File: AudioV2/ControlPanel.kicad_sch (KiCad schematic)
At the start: 39 parts, among them SW1 PWR SW, SW501 DEST sense (3PDT 3rd pole), U501 Pico 2 / RP2350, U502 PT2314-D, U503 BP5293-50 +5V

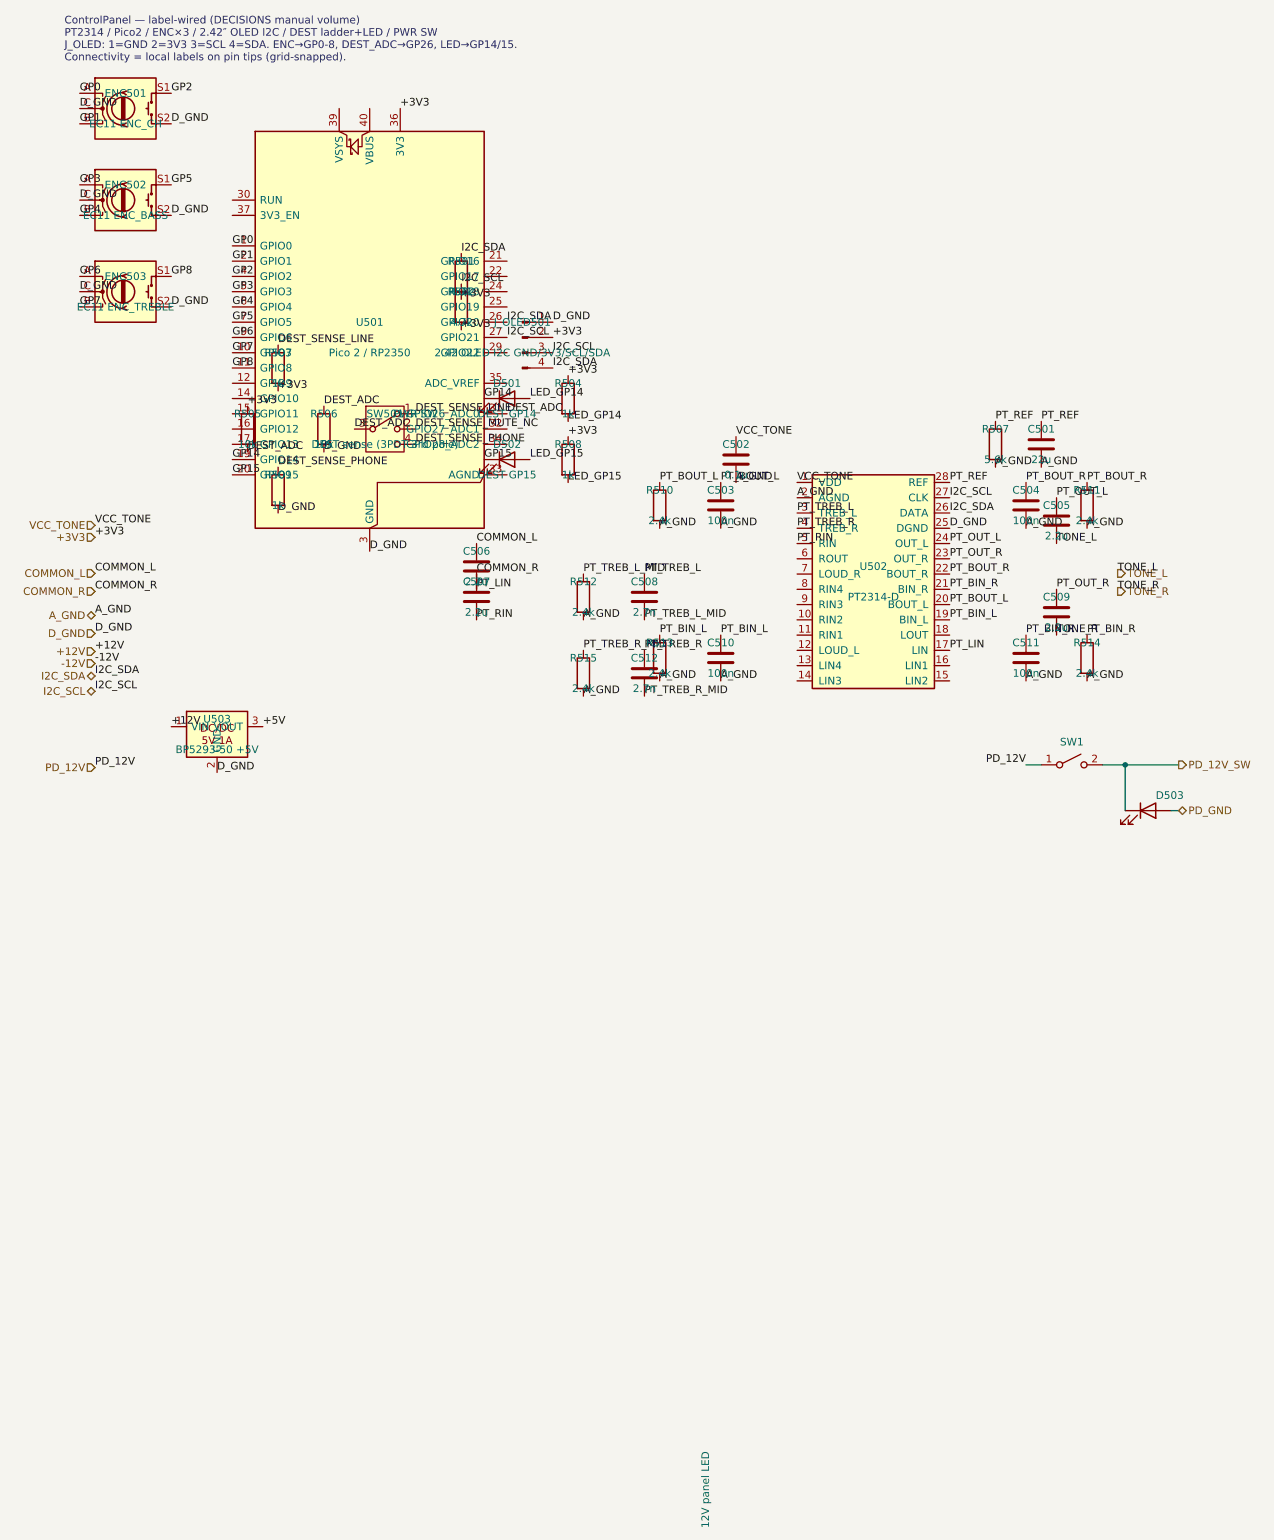
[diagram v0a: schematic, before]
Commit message: AudioV2: Amp再版とRelayBoard本配線、番地ストラップを0Ω化
高速オペアンプを差せるようAmpをバルク対応で再版した（ゲイン2＝20k/20k、
±12V、100µF/rail + 100nF + 1nF、DIP-8ソケット）。親には代表1シートだけ置き、
物理は同一仕様×10製造とする。PCBは既存基板の端子・4穴を維持したまま上辺を
15mm拡張してバルクを載せた。

RelayBoardは未給電Ampへ信号を印加しないよう、Amp入力と±12Vを同一の
SET/RESETで同時切替する構成で本配線した。番地はA1/A0の0Ωストラップで
0x20–0x23を選び、1枚のPCB設計を最大4枚に使い回す。SolderJumperは
FPが1.3mmピッチで0Ωチップが載らないため1206パッドに変更した。
プルダウン10kΩはジャンパ後段に置き常時実装（手前分岐だと未実装時に
A0/A1が浮く）。

ERC 207→56。Power/Output/Amp/Relay A・B は0件で、残りはControlの
未使用ピンと親の箱外ラベル。AmpのPCB DRCは電気エラー0・未配線0。

レビュー指摘（IC直近パスコン、AZ850のset voltage余裕、A0/A1ネット無名）は
未対応でAGENT_HANDOFF §2.7に記録。addr_strapのスクリプト側は現図と
非同期なので、同期までwire_circuit_design.py relayを回さない。

Co-authored-by: Cursor <cursoragent@cursor.com>
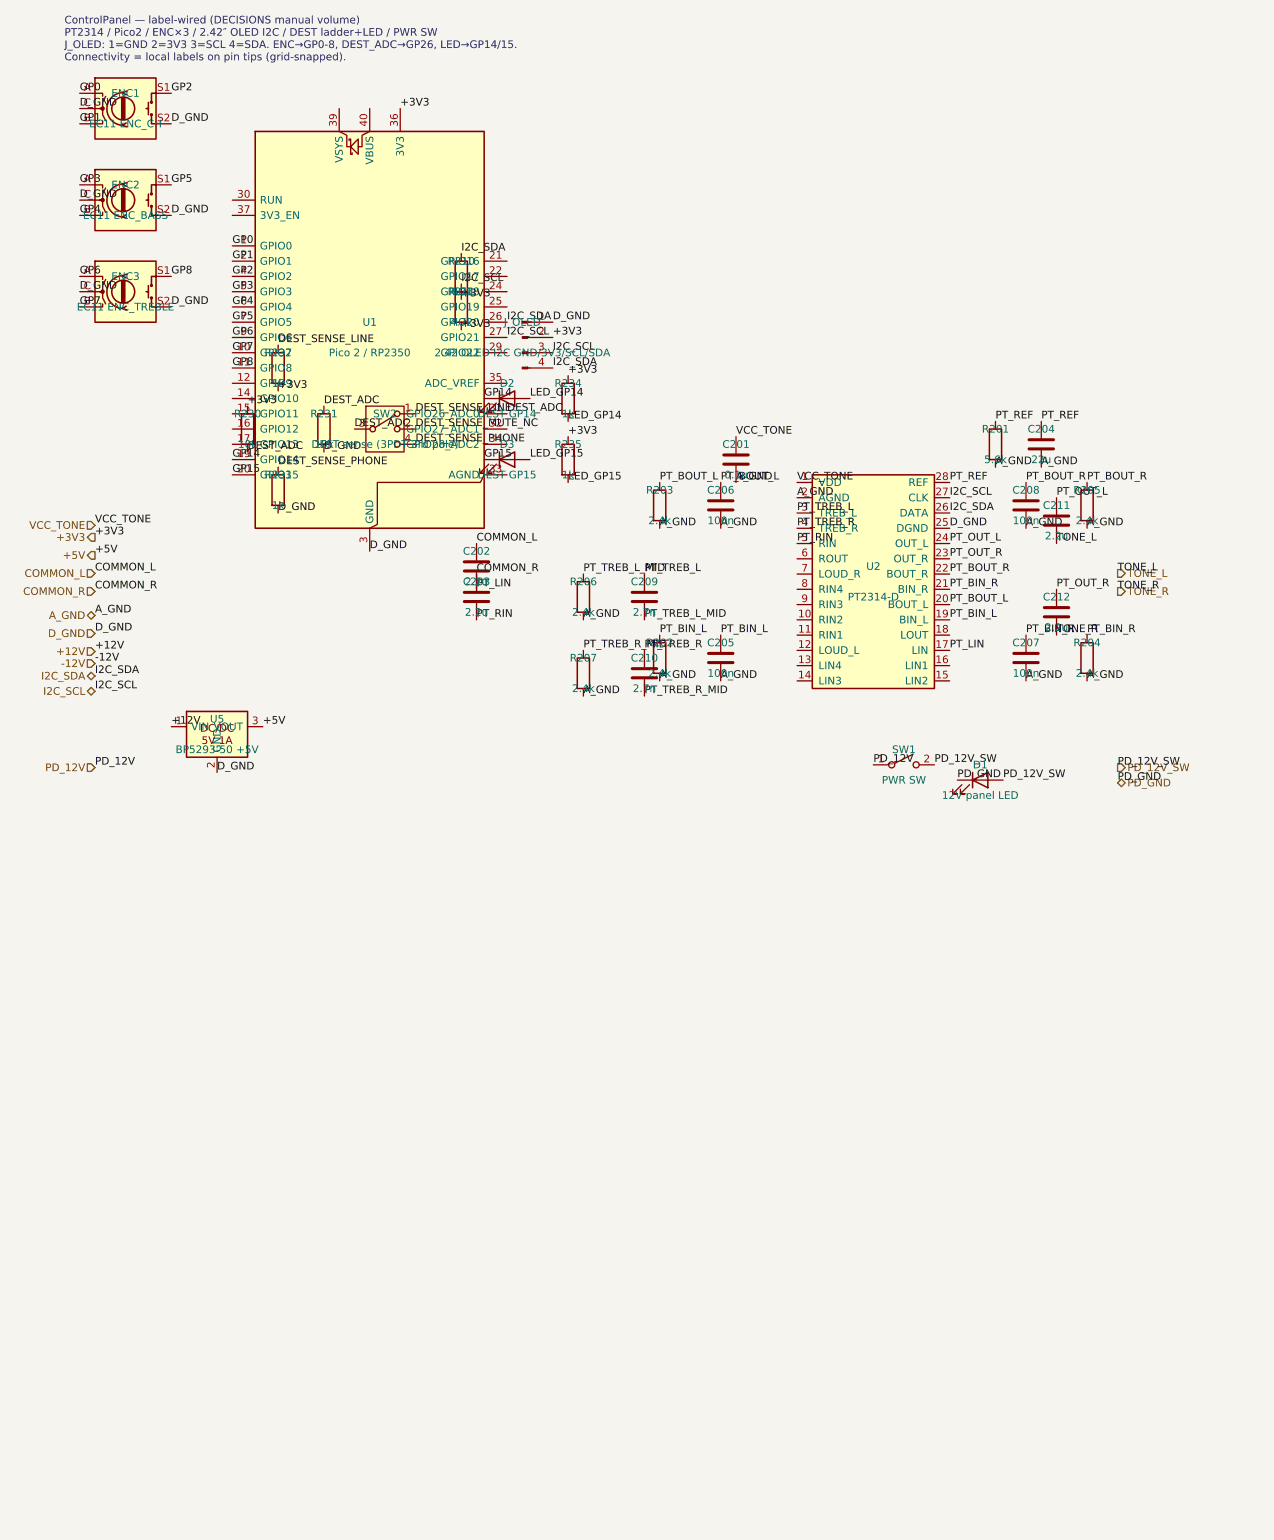
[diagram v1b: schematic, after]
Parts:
- removed C501: 22u, symbol Device:C
- removed C502: 0.1u, symbol Device:C
- removed C503, C504, C510, C511: 100n, symbol Device:C
- removed C505, C506, C507, C509: 2.2u, symbol Device:C
- removed C508, C512: 2.7n, symbol Device:C
- removed D501: DEST GP14, symbol Device:LED
- removed D502: DEST GP15, symbol Device:LED
- removed D503: 12V panel LED, symbol Device:LED
- removed ENC501: EC11 ENC_CH, symbol Device:RotaryEncoder_Switch
- removed ENC502: EC11 ENC_BASS, symbol Device:RotaryEncoder_Switch
- removed ENC503: EC11 ENC_TREBLE, symbol Device:RotaryEncoder_Switch
- removed J_OLED501: 2.42 OLED I2C GND/3V3/SCL/SDA, symbol Connector:Conn_01x04_Pin
- removed R501, R502: 4.7k, symbol Device:R
- removed R503, R504, R508, R509: 1k, symbol Device:R
- removed R505, R506: 10k, symbol Device:R
- removed R507: 5.6k, symbol Device:R
- removed R510, R511, R512, R513, R514, R515: 2.4k, symbol Device:R
- removed SW501: DEST sense (3PDT 3rd pole), symbol Switch:SW_SP3T
- removed U501: Pico 2 / RP2350, symbol MCU_Module:RaspberryPi_Pico
- removed U502: PT2314-D, symbol AudioV2:PT2314
- removed U503: BP5293-50 +5V, symbol BP5293_ROHM:BP5293-50
- added C201: 0.1u, symbol Device:C
- added C202, C203, C211, C212: 2.2u, symbol Device:C
- added C204: 22u, symbol Device:C
- added C205, C206, C207, C208: 100n, symbol Device:C
- added C209, C210: 2.7n, symbol Device:C
- added D1: 12V panel LED, symbol Device:LED
- added D2: DEST GP14, symbol Device:LED
- added D3: DEST GP15, symbol Device:LED
- added ENC1: EC11 ENC_CH, symbol Device:RotaryEncoder_Switch
- added ENC2: EC11 ENC_BASS, symbol Device:RotaryEncoder_Switch
- added ENC3: EC11 ENC_TREBLE, symbol Device:RotaryEncoder_Switch
- added J_OLED: 2.42 OLED I2C GND/3V3/SCL/SDA, symbol Connector:Conn_01x04_Pin
- added R201: 5.6k, symbol Device:R
- added R202, R203, R204, R205, R206, R207: 2.4k, symbol Device:R
- added R210, R211: 4.7k, symbol Device:R
- added R230, R231: 10k, symbol Device:R
- added R232, R233, R234, R235: 1k, symbol Device:R
- added SW2: DEST sense (3PDT 3rd pole), symbol Switch:SW_SP3T
- added U1: Pico 2 / RP2350, symbol MCU_Module:RaspberryPi_Pico
- added U2: PT2314-D, symbol AudioV2:PT2314
- added U5: BP5293-50 +5V, symbol BP5293_ROHM:BP5293-50
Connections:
- net +12V: now also U5.1 (VIN)
- net +3V3: now also J_OLED.2 (Pin_2), R210.2, R211.2, R230.1, R232.2, R234.1, R235.1, U1.36 (3V3)
- net +5V: now also U5.3 (VOUT)
- net A_GND: now also C201.2, C204.2, C205.2, C206.2, C207.2, C208.2, R201.2, R202.2, R203.2, R204.2, R205.2, R206.2, R207.2, U2.2 (AGND)
- net COMMON_L: now also C202.1
- net COMMON_R: now also C203.1
- net DEST_ADC: now also R230.2, R231.1, SW2.3, U1.31 (GPIO26_ADC0)
- net DEST_SENSE_LINE: now also R232.1, SW2.1
- net DEST_SENSE_MUTE_NC: now also SW2.2
- net DEST_SENSE_PHONE: now also R233.1, SW2.4
- net D_GND: now also ENC1.C, ENC1.S2, ENC2.C, ENC2.S2, ENC3.C, ENC3.S2, J_OLED.1 (Pin_1), R231.2, R233.2, U1.13 (GND), U1.18 (GND), U1.23 (GND), U1.28 (GND), U1.3 (GND), U1.38 (GND), U1.8 (GND), U2.25 (DGND), U5.2 (GND)
- net GP0: now also ENC1.A, U1.1 (GPIO0)
- net GP1: now also ENC1.B, U1.2 (GPIO1)
- net GP14: now also D2.1 (K), U1.19 (GPIO14)
- net GP15: now also D3.1 (K), U1.20 (GPIO15)
- net GP2: now also ENC1.S1, U1.4 (GPIO2)
- net GP3: now also ENC2.A, U1.5 (GPIO3)
- net GP4: now also ENC2.B, U1.6 (GPIO4)
- net GP5: now also ENC2.S1, U1.7 (GPIO5)
- net GP6: now also ENC3.A, U1.9 (GPIO6)
- net GP7: now also ENC3.B, U1.10 (GPIO7)
- net GP8: now also ENC3.S1, U1.11 (GPIO8)
- net I2C_SCL: now also J_OLED.3 (Pin_3), R211.1, U1.27 (GPIO21), U2.27 (CLK)
- net I2C_SDA: now also J_OLED.4 (Pin_4), R210.1, U1.26 (GPIO20), U2.26 (DATA)
- net LED_GP14: now also D2.2 (A), R234.2
- net LED_GP15: now also D3.2 (A), R235.2
- net PD_12V_SW: now also D1.2 (A)
- net PD_GND: now also D1.1 (K)
- net PT_BIN_L: now also C205.1, R202.1, U2.19 (BIN_L)
- net PT_BIN_R: now also C207.1, R204.1, U2.21 (BIN_R)
- net PT_BOUT_L: now also C206.1, R203.1, U2.20 (BOUT_L)
- net PT_BOUT_R: now also C208.1, R205.1, U2.22 (BOUT_R)
- net PT_LIN: now also C202.2, U2.17 (LIN)
- net PT_OUT_L: now also C211.1, U2.24 (OUT_L)
- net PT_OUT_R: now also C212.1, U2.23 (OUT_R)
- net PT_REF: now also C204.1, R201.1, U2.28 (REF)
- net PT_RIN: now also C203.2, U2.5 (RIN)
- net PT_TREB_L: now also C209.1, U2.3 (TREB_L)
- net PT_TREB_L_MID: now also C209.2, R206.1
- net PT_TREB_R: now also C210.1, U2.4 (TREB_R)
- net PT_TREB_R_MID: now also C210.2, R207.1
- net TONE_L: now also C211.2
- net TONE_R: now also C212.2
- net VCC_TONE: now also C201.1, U2.1 (VDD)
